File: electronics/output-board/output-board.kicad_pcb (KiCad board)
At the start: 0 parts

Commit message: Finished Schematic and Started Routing the Output Board
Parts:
- added C1: 1uF, Capacitor_SMD:C_0603_1608Metric, F.Cu at (16.4, 69.0)
- added C10: 100nF, Capacitor_SMD:C_0603_1608Metric, F.Cu at (43.5, 57.3)
- added C11: 100nF, Capacitor_SMD:C_0603_1608Metric, F.Cu at (142.2, 81.3)
- added C12: 100nF, Capacitor_SMD:C_0603_1608Metric, F.Cu at (40.4, 54.8)
- added C13: 100nF, Capacitor_SMD:C_0603_1608Metric, F.Cu at (39.5, 57.3)
- added C14: 100nF, Capacitor_SMD:C_0603_1608Metric, F.Cu at (40.4, 49.8)
- added C15: 100nF, Capacitor_SMD:C_0603_1608Metric, F.Cu at (32.0, 67.0)
- added C16: 100nF, Capacitor_SMD:C_0603_1608Metric, F.Cu at (44.4, 54.8)
- added C17: 100nF, Capacitor_SMD:C_0603_1608Metric, F.Cu at (44.4, 52.3)
- added C18: 100nF, Capacitor_SMD:C_0603_1608Metric, F.Cu at (20.4, 69.0)
- added C19: 100nF, Capacitor_SMD:C_0603_1608Metric, F.Cu at (31.5, 59.5)
- added C2: 10nF, Capacitor_SMD:C_0603_1608Metric, F.Cu at (40.4, 52.3)
- added C20: 100nF, Capacitor_SMD:C_0603_1608Metric, F.Cu at (39.5, 62.3)
- added C21: 100nF, Capacitor_SMD:C_0603_1608Metric, F.Cu at (35.5, 62.0)
- added C3: 1uF, Capacitor_SMD:C_0603_1608Metric, F.Cu at (48.4, 49.8)
- added C4: 20pF, Capacitor_SMD:C_0603_1608Metric, F.Cu at (35.5, 59.5)
- added C5: 20pF, Capacitor_SMD:C_0603_1608Metric, F.Cu at (35.1, 57.0)
- added C6: 100nF, Capacitor_SMD:C_0603_1608Metric, F.Cu at (48.4, 54.8)
- added C7: 2.2uF, Capacitor_SMD:C_0603_1608Metric, F.Cu at (39.5, 59.8)
- added C8: 2.2uF, Capacitor_SMD:C_0603_1608Metric, F.Cu at (35.5, 64.5)
- added C9: 100nF, Capacitor_SMD:C_0603_1608Metric, F.Cu at (139.2, 81.3)
- added D1: LED, LED_SMD:LED_1206_3216Metric, F.Cu at (53.8, 26.2)
- added D10: LED, LED_SMD:LED_1206_3216Metric, F.Cu at (45.9, 94.6)
- added D11: LED, LED_SMD:LED_1206_3216Metric, F.Cu at (65.2, 83.5)
- added D12: LED, LED_SMD:LED_1206_3216Metric, F.Cu at (69.4, 55.0)
- added D13: LED, LED_SMD:LED_1206_3216Metric, F.Cu at (26.7, 80.3)
- added D2: LED, LED_SMD:LED_1206_3216Metric, F.Cu at (16.8, 39.9)
- added D3: LED, LED_SMD:LED_1206_3216Metric, F.Cu at (90.2, 42.2)
- added D4: LED, LED_SMD:LED_1206_3216Metric, F.Cu at (130.0, 55.5)
- added D5: LED, LED_SMD:LED_1206_3216Metric, F.Cu at (69.4, 69.3)
- added D6: LED, LED_SMD:LED_1206_3216Metric, F.Cu at (45.9, 80.3)
- added D7: LED, LED_SMD:LED_1206_3216Metric, F.Cu at (88.6, 69.3)
- added D8: LED, LED_SMD:LED_1206_3216Metric, F.Cu at (107.9, 55.0)
- added D9: LED, LED_SMD:LED_1206_3216Metric, F.Cu at (88.6, 55.0)
- added J1: Conn_01x02_Male, Connector_Molex:Molex_SL_171971-0002_1x02_P2.54mm_Vertical, F.Cu at (49.8, 16.0)
- added J10: Conn_01x02_Male, Connector_Molex:Molex_SL_171971-0002_1x02_P2.54mm_Vertical, F.Cu at (79.8, 66.3)
- added J11: Conn_01x02_Male, Connector_Molex:Molex_SL_171971-0002_1x02_P2.54mm_Vertical, F.Cu at (99.0, 52.1)
- added J12: Conn_01x02_Male, Connector_Molex:Molex_SL_171971-0002_1x02_P2.54mm_Vertical, F.Cu at (79.8, 52.1)
- added J13: Conn_01x02_Male, Connector_Molex:Molex_SL_171971-0002_1x02_P2.54mm_Vertical, F.Cu at (37.1, 91.7)
- added J14: Arming switch, Connector_PinHeader_2.54mm:PinHeader_1x02_P2.54mm_Vertical, F.Cu at (27.1, 60.9)
- added J15: Conn_01x02_Male, Connector_Molex:Molex_SL_171971-0002_1x02_P2.54mm_Vertical, F.Cu at (56.3, 80.6)
- added J16: Conn_01x02_Male, Connector_Molex:Molex_SL_171971-0002_1x02_P2.54mm_Vertical, F.Cu at (60.5, 52.1)
- added J17: Conn_01x02_Male, Connector_Molex:Molex_SL_171971-0002_1x02_P2.54mm_Vertical, F.Cu at (17.9, 77.4)
- added J18: Conn_01x02_Male, Connector_Molex:Molex_SL_171971-0002_1x02_P2.54mm_Vertical, F.Cu at (17.4, 33.1)
- added J2: Conn_01x02_Male, Connector_Molex:Molex_SL_171971-0002_1x02_P2.54mm_Vertical, F.Cu at (81.3, 39.2)
- added J3: 12V In, Connector_PinHeader_2.54mm:PinHeader_1x02_P2.54mm_Vertical, F.Cu at (39.4, 19.3)
- added J4: Conn_01x02, Connector_PinHeader_2.54mm:PinHeader_1x02_P2.54mm_Vertical, F.Cu at (36.1, 50.8)
- added J5: SWD Header, Connector_PinHeader_2.54mm:PinHeader_1x04_P2.54mm_Vertical, F.Cu at (16.7, 50.8)
- added J6: Conn_01x02, Connector_PinHeader_2.54mm:PinHeader_1x02_P2.54mm_Vertical, F.Cu at (31.4, 50.8)
- added J7: Conn_01x02_Male, Connector_Molex:Molex_SL_171971-0002_1x02_P2.54mm_Vertical, F.Cu at (121.2, 52.6)
- added J8: Conn_01x02_Male, Connector_Molex:Molex_SL_171971-0002_1x02_P2.54mm_Vertical, F.Cu at (60.5, 66.3)
- added J9: Conn_01x02_Male, Connector_Molex:Molex_SL_171971-0002_1x02_P2.54mm_Vertical, F.Cu at (37.1, 77.4)
- added L1: 10uH, Inductor_SMD:L_0603_1608Metric, F.Cu at (31.5, 64.5)
- added MOSFET1: BSS806NEH6327XTSA1, MOSFET:BSS806NEH6327XTSA1, F.Cu at (48.8, 23.1)
- added MOSFET10: BUK9Y21-40E, MOSFET 2:BUK9Y21-40E, F.Cu at (27.7, 93.2)
- added MOSFET11: BSS806NEH6327XTSA1, MOSFET:BSS806NEH6327XTSA1, F.Cu at (65.8, 79.4)
- added MOSFET12: BSS806NEH6327XTSA1, MOSFET:BSS806NEH6327XTSA1, F.Cu at (70.0, 50.9)
- added MOSFET13: BSS806NEH6327XTSA1, MOSFET:BSS806NEH6327XTSA1, F.Cu at (27.3, 76.2)
- added MOSFET18: BSS806NEH6327XTSA1, MOSFET:BSS806NEH6327XTSA1, F.Cu at (26.9, 31.9)
- added MOSFET2: BSS806NEH6327XTSA1, MOSFET:BSS806NEH6327XTSA1, F.Cu at (90.8, 38.1)
- added MOSFET3: BSS806NEH6327XTSA1, MOSFET:BSS806NEH6327XTSA1, F.Cu at (130.6, 51.4)
- added MOSFET4: BSS806NEH6327XTSA1, MOSFET:BSS806NEH6327XTSA1, F.Cu at (70.0, 65.2)
- added MOSFET5: BSS806NEH6327XTSA1, MOSFET:BSS806NEH6327XTSA1, F.Cu at (46.5, 76.2)
- added MOSFET6: BSS806NEH6327XTSA1, MOSFET:BSS806NEH6327XTSA1, F.Cu at (89.2, 65.2)
- added MOSFET7: BSS806NEH6327XTSA1, MOSFET:BSS806NEH6327XTSA1, F.Cu at (108.5, 50.9)
- added MOSFET8: BSS806NEH6327XTSA1, MOSFET:BSS806NEH6327XTSA1, F.Cu at (89.2, 50.9)
- added MOSFET9: BSS806NEH6327XTSA1, MOSFET:BSS806NEH6327XTSA1, F.Cu at (46.5, 90.5)
- added R1: 0k, Resistor_SMD:R_0603_1608Metric, F.Cu at (48.4, 52.3)
- added R10: 500, Resistor_SMD:R_0603_1608Metric, F.Cu at (82.4, 58.4)
- added R11: 500, Resistor_SMD:R_0603_1608Metric, F.Cu at (39.7, 98.0)
- added R12: 1K, Resistor_SMD:R_0603_1608Metric, F.Cu at (31.1, 57.0)
- added R13: 100K, Resistor_SMD:R_0603_1608Metric, F.Cu at (32.0, 69.5)
- added R14: 1K, Resistor_SMD:R_0603_1608Metric, F.Cu at (74.1, 78.3)
- added R15: 1K, Resistor_SMD:R_0603_1608Metric, F.Cu at (48.8, 27.2)
- added R16: 1K, Resistor_SMD:R_0603_1608Metric, F.Cu at (95.1, 36.9)
- added R17: 1K, Resistor_SMD:R_0603_1608Metric, F.Cu at (134.9, 50.3)
- added R18: 1K, Resistor_SMD:R_0603_1608Metric, F.Cu at (59.1, 72.7)
- added R19: 1K, Resistor_SMD:R_0603_1608Metric, F.Cu at (35.7, 83.8)
- added R2: 500, Resistor_SMD:R_0603_1608Metric, F.Cu at (54.4, 22.4)
- added R20: 500, Resistor_SMD:R_0603_1608Metric, F.Cu at (25.4, 35.6)
- added R21: 1K, Resistor_SMD:R_0603_1608Metric, F.Cu at (78.3, 72.7)
- added R22: 1K, Resistor_SMD:R_0603_1608Metric, F.Cu at (97.6, 58.4)
- added R23: 1K, Resistor_SMD:R_0603_1608Metric, F.Cu at (78.3, 58.4)
- added R24: 1K, Resistor_SMD:R_0603_1608Metric, F.Cu at (35.7, 98.0)
- added R25: 1K, Resistor_SMD:R_0603_1608Metric, F.Cu at (54.9, 86.9)
- added R26: 500, Resistor_SMD:R_0603_1608Metric, F.Cu at (58.9, 86.9)
- added R27: 1K, Resistor_SMD:R_0603_1608Metric, F.Cu at (59.1, 58.4)
- added R28: 500, Resistor_SMD:R_0603_1608Metric, F.Cu at (63.1, 58.4)
- added R29: 1K, Resistor_SMD:R_0603_1608Metric, F.Cu at (16.4, 83.8)
- added R3: 10k, Resistor_SMD:R_0603_1608Metric, F.Cu at (31.5, 62.0)
- added R30: 500, Resistor_SMD:R_0603_1608Metric, F.Cu at (20.4, 83.8)
- added R4: 500, Resistor_SMD:R_0603_1608Metric, F.Cu at (89.3, 45.1)
- added R5: 500, Resistor_SMD:R_0603_1608Metric, F.Cu at (129.1, 58.4)
- added R6: 500, Resistor_SMD:R_0603_1608Metric, F.Cu at (63.1, 72.7)
- added R7: 500, Resistor_SMD:R_0603_1608Metric, F.Cu at (39.7, 83.8)
- added R8: 500, Resistor_SMD:R_0603_1608Metric, F.Cu at (82.4, 72.7)
- added R9: 500, Resistor_SMD:R_0603_1608Metric, F.Cu at (101.6, 58.4)
- added SW1: SW_Push_Dual, RESET BUTTON:Button CS1102, F.Cu at (19.6, 64.3)
- added U1: MAX33012EASA+, MAX33012EASA+:MAX33012EASA+, F.Cu at (56.4, 42.4)
- added U2: LD3985M33R_SOT23, Package_TO_SOT_SMD:SOT-23-5, F.Cu at (27.4, 68.0)
- added U3: STM32F446ZEHx, Package_BGA:UFBGA-144_7x7mm_Layout12x12_P0.5mm, F.Cu at (142.2, 88.9)
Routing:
- net Net-(D1-Pad1): track 0.00 -> 14.7 mm
- net +12V: track 0.00 -> 9.62 mm
- net Net-(D1-Pad2): track 0.00 -> 3.84 mm
- net Net-(MOSFET1-Pad1): track 0.00 -> 2.78 mm
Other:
- copper layers 0 -> 2

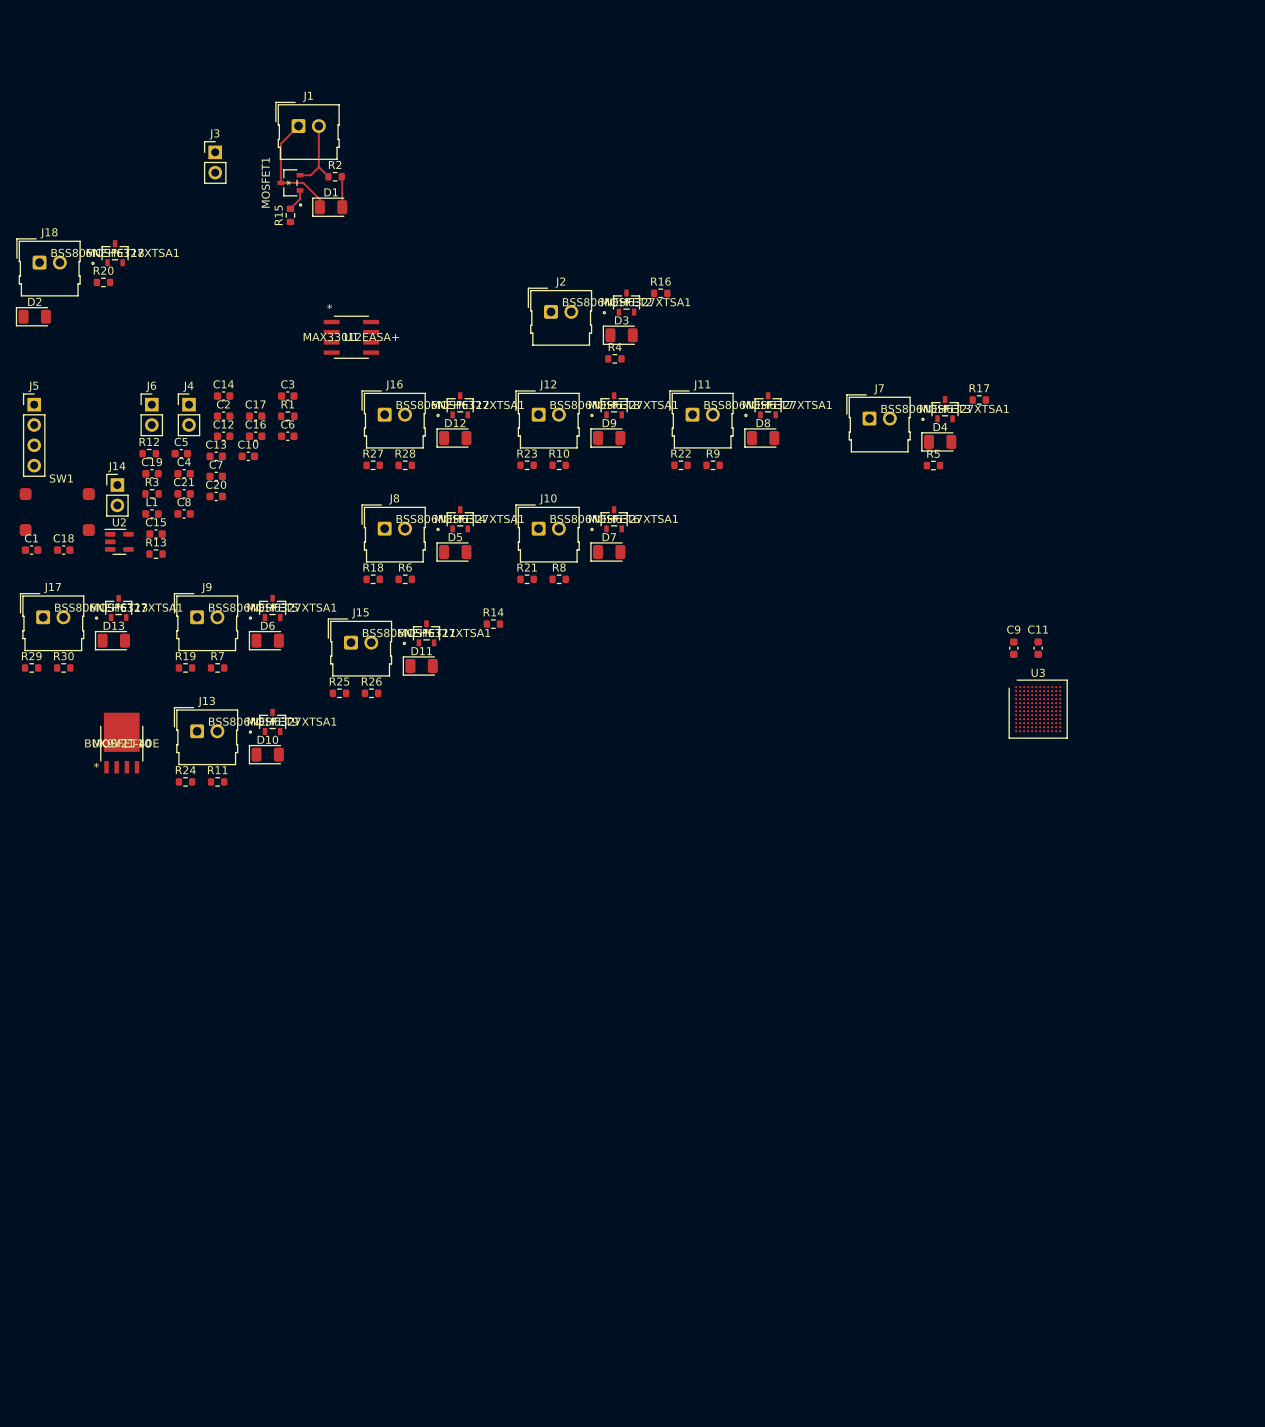
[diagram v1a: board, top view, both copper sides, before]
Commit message: Output Board is basically done!
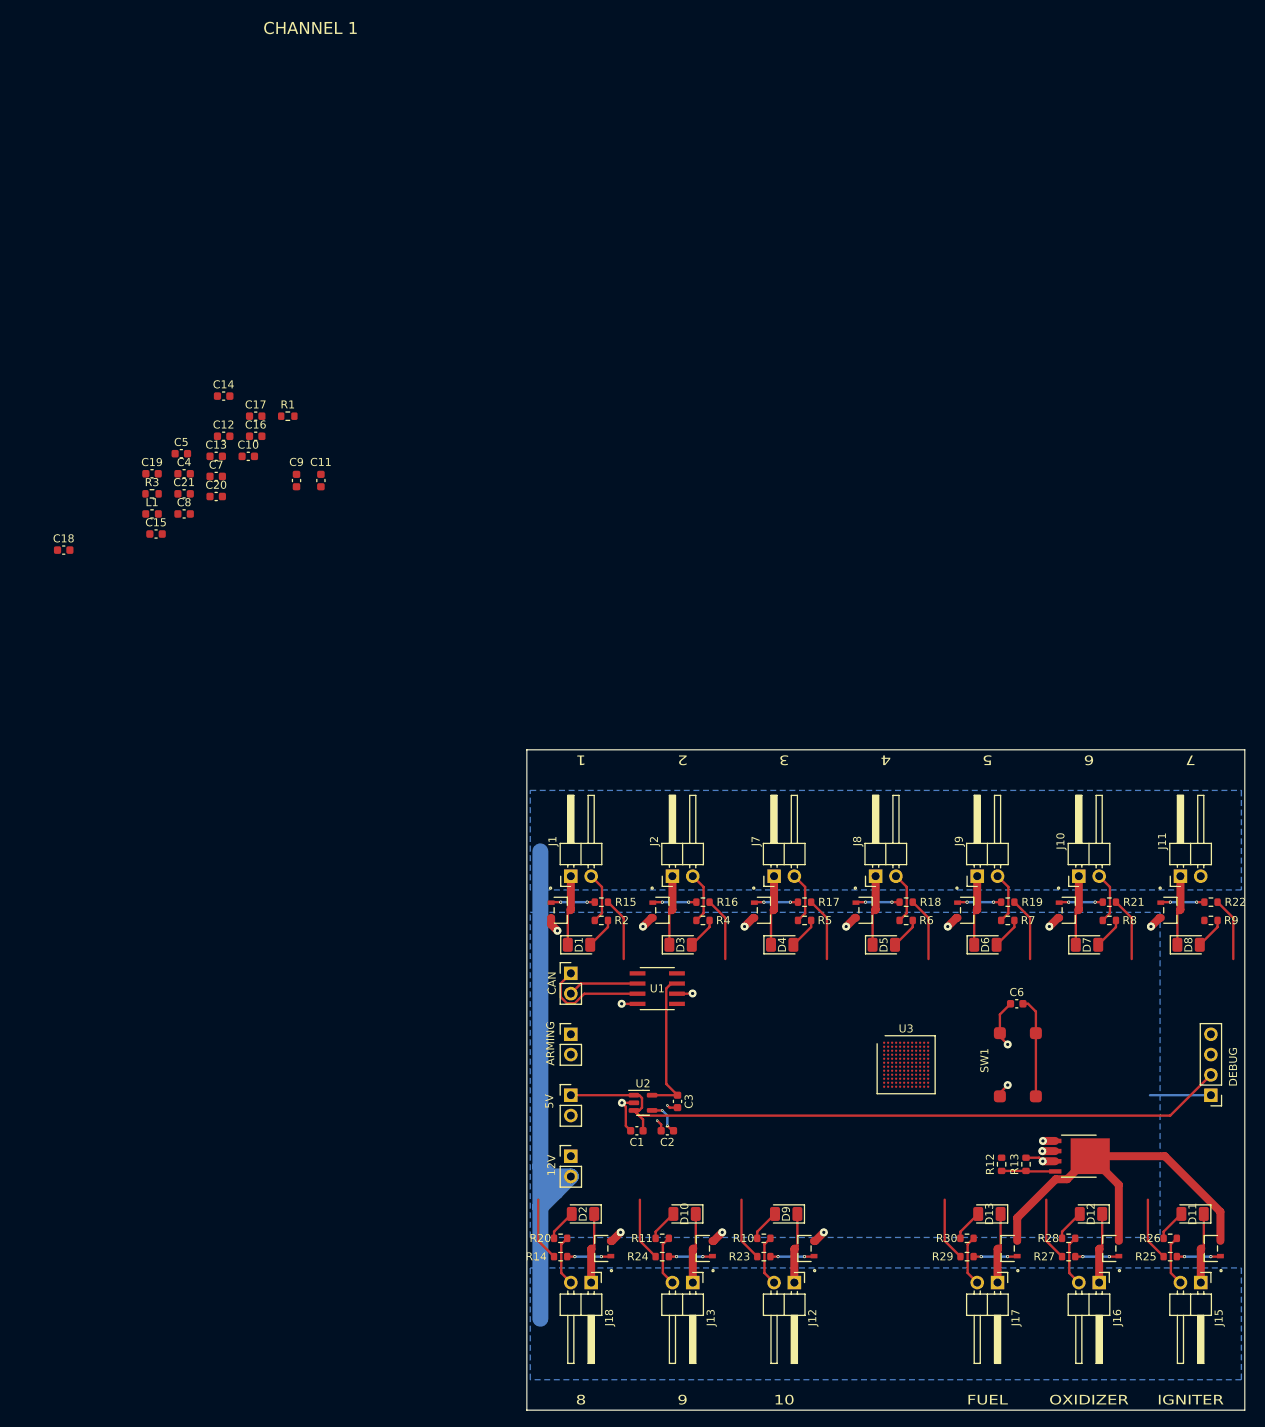
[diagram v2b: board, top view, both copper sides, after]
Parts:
- J1, J10, J11, J12, J13, J15, J16, J17, J18, J2, J7, J8, J9: footprint Connector_Molex:Molex_SL_171971-0002_1x02_P2.54mm_Vertical -> Connector_PinHeader_2.54mm:PinHeader_1x02_P2.54mm_Horizontal
- J14: value Arming switch -> ARMING
- J3: value 12V In -> 12V
- J4: value Conn_01x02 -> 5V
- J5: value SWD Header -> DEBUG
- J6: value Conn_01x02 -> CAN
- moved J5 170.5 mm to (163.8, 137.2), turned to 180 degrees
- moved J17 145.4 mm to (137.2, 160.6), turned to -90 degrees
- moved J18 144.9 mm to (86.4, 160.6), turned to -90 degrees
- moved J16 140.5 mm to (149.9, 160.6), turned to -90 degrees
- moved R12 138.7 mm to (137.7, 145.8), turned to 90 degrees
- moved SW1 138.5 mm to (139.7, 133.3), turned to 90 degrees
- moved MOSFET18 138.5 mm to (87.6, 156.3), turned to 90 degrees
- moved R29 138.2 mm to (133.3, 157.3)
- moved MOSFET13 137.0 mm to (138.4, 156.3), turned to 90 degrees
- moved R30 133.5 mm to (133.3, 155.0), turned to 180 degrees
- moved J3 133.1 mm to (83.8, 144.8)
- moved MOSFET12 133.0 mm to (151.1, 156.3), turned to 90 degrees
- moved J15 133.0 mm to (162.6, 160.6), turned to -90 degrees
- moved R13 132.8 mm to (140.7, 145.8), turned to 90 degrees
- moved R20 132.5 mm to (82.5, 155.0), turned to 180 degrees
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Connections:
- MOSFET1 pad 2: +12V -> GND
- MOSFET18 pad 2: +12V -> GND
- MOSFET2 pad 2: +12V -> GND
- MOSFET3 pad 2: +12V -> GND
- MOSFET4 pad 2: +12V -> GND
- MOSFET5 pad 2: +12V -> GND
- MOSFET6 pad 2: +12V -> GND
- MOSFET7 pad 2: +12V -> GND
- MOSFET8 pad 2: +12V -> GND
- MOSFET9 pad 2: +12V -> GND
- R13 pad 1: Net-(J14-Pad1) -> Net-(MOSFET10-Pad4)
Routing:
- net +12V: track 9.62 -> 147.1 mm
- net +5V: track 0.00 -> 88.9 mm
- net GND: track 0.00 -> 51.7 mm, vias 0 -> 20
- net /Ignition MOSFET/GROUND: track 0.00 -> 50.1 mm
- net +3V3: track 0.00 -> 18.7 mm
- net Net-(J6-Pad1): track 0.00 -> 13.9 mm
- net Net-(C6-Pad2): track 0.00 -> 12.6 mm
- net Net-(J6-Pad2): track 0.00 -> 8.86 mm
- net Net-(D2-Pad1): track 0.00 -> 8.74 mm
- net Net-(D8-Pad1): track 0.00 -> 8.74 mm
- net Net-(D12-Pad1): track 0.00 -> 8.74 mm
- net Net-(D9-Pad1): track 0.00 -> 8.74 mm
- net Net-(D13-Pad1): track 0.00 -> 8.74 mm
- net Net-(D11-Pad1): track 0.00 -> 8.74 mm
- net Net-(D10-Pad1): track 0.00 -> 8.74 mm
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- added copper zone on B.Cu, net +12V
- added copper zone on B.Cu, net GND
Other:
- board outline added: 89.7 x 82.5 mm
- board text added: "1"
- board text added: "10"
- board text added: "2"
- board text added: "3"
- board text added: "4"
- board text added: "5"
- board text added: "6"
- board text added: "7"
- board text added: "8"
- board text added: "9"
- board text added: "CHANNEL 1"
- board text added: "FUEL"
- board text added: "IGNITER"
- board text added: "OXIDIZER"

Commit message: Put in connectors and finalized layout of everything except MCU.
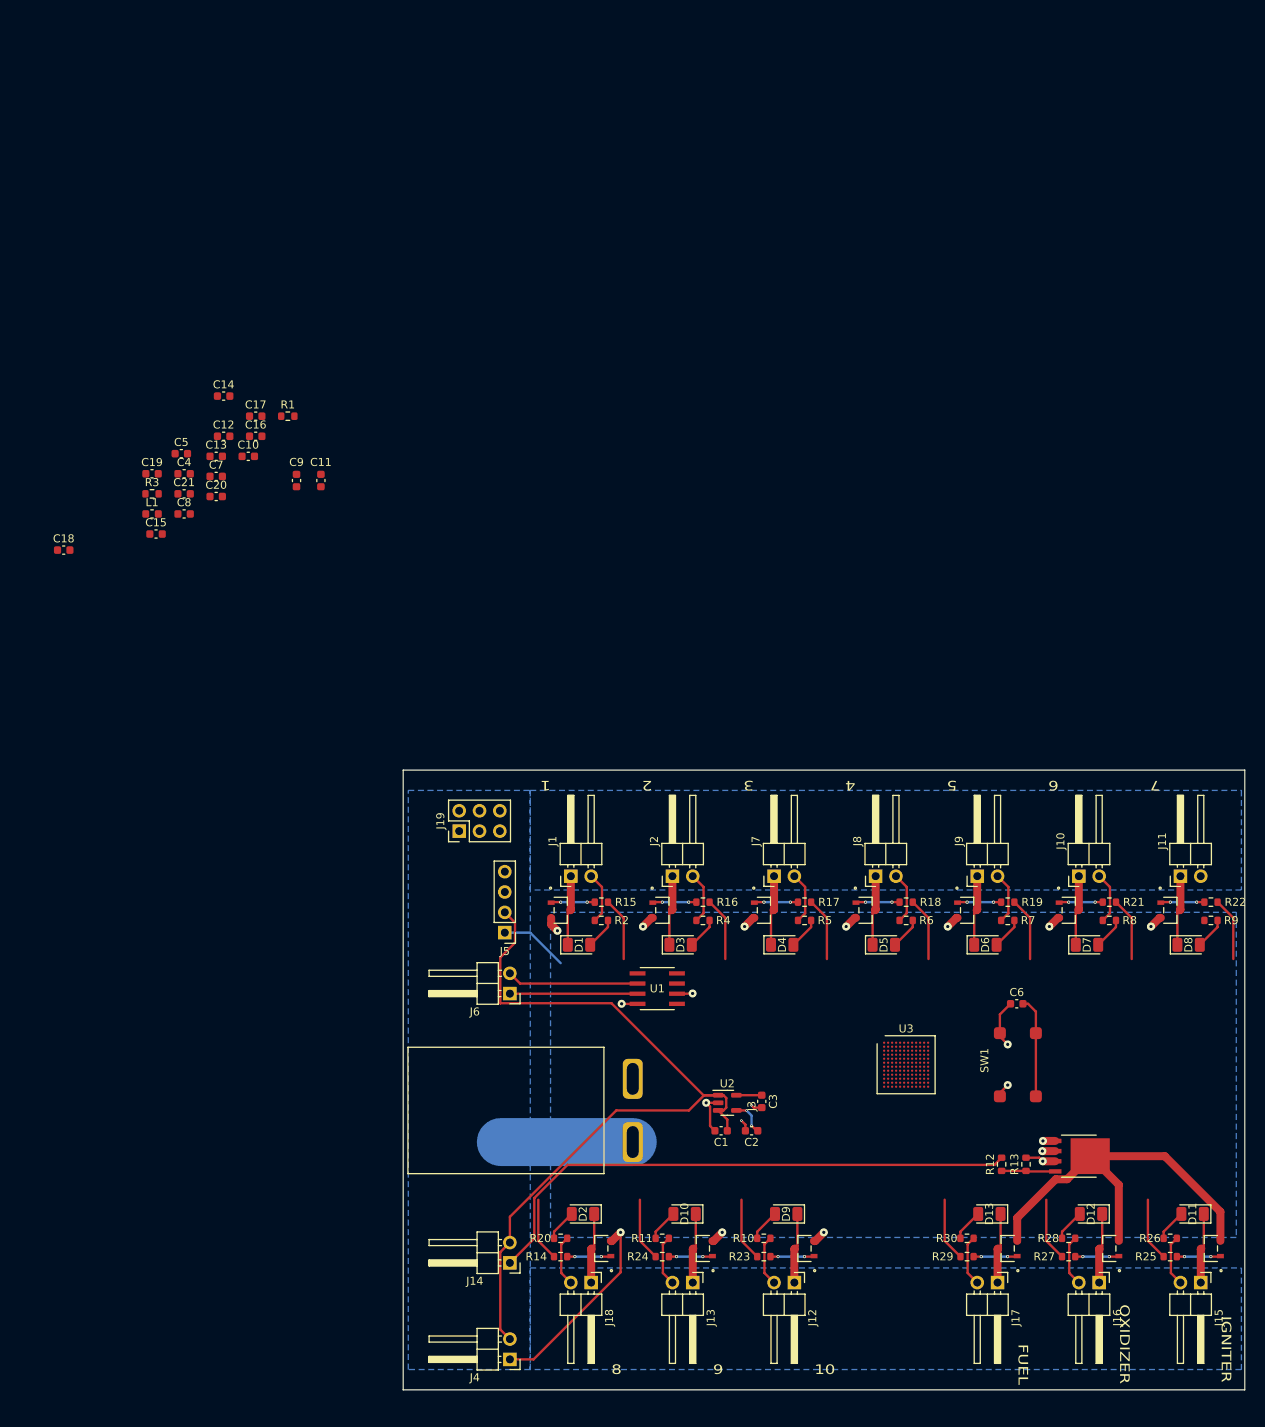
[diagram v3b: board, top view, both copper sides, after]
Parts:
- added J19: Extra IO, Connector_PinHeader_2.54mm:PinHeader_2x03_P2.54mm_Vertical, F.Cu at (69.9, 104.1)
- J1, J10, J11, J12, J13, J15, J16, J17, J18, J2, J7, J8, J9: footprint Connector_PinHeader_2.54mm:PinHeader_1x02_P2.54mm_Horizontal -> CustomFootprints:LatchingConnector2POS
- J14: value ARMING -> Arming switch; footprint Connector_PinHeader_2.54mm:PinHeader_1x02_P2.54mm_Vertical -> CustomFootprints:LatchingConnector2POS
- J3: value 12V -> 12V In; footprint Connector_PinHeader_2.54mm:PinHeader_1x02_P2.54mm_Vertical -> CustomFootprints:PowerPoleThroughHole
- J4: value 5V -> Conn_01x02; footprint Connector_PinHeader_2.54mm:PinHeader_1x02_P2.54mm_Vertical -> CustomFootprints:LatchingConnector2POS
- J5: value DEBUG -> SWD Header
- J6: value CAN -> Conn_01x02; footprint Connector_PinHeader_2.54mm:PinHeader_1x02_P2.54mm_Vertical -> CustomFootprints:LatchingConnector2POS
- moved J5 90.6 mm to (75.6, 116.8)
- moved J4 33.9 mm to (76.2, 170.2), turned to 180 degrees
- moved J14 29.6 mm to (76.2, 158.1), turned to 180 degrees
- moved C1 10.5 mm to (102.6, 141.6)
- moved C2 10.5 mm to (106.4, 141.6)
- moved C3 10.5 mm to (107.7, 137.9)
- moved U2 10.5 mm to (103.4, 138.1)
- moved J3 9.62 mm to (91.6, 139.1), turned to 90 degrees
- moved J6 8.03 mm to (76.2, 124.5), turned to 180 degrees
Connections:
- J4 pad 1: +5V -> GND
- J4 pad 2: GND -> +5V
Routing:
- net Net-(J14-Pad1): track 0.00 -> 69.9 mm
- net +12V: track 147.1 -> 93.3 mm
- net GND: track 51.7 -> 76.0 mm
- net +3V3: track 18.7 -> 3.17 mm
- net +5V: track 88.9 -> 99.8 mm
- net Net-(J6-Pad2): track 8.86 -> 16.5 mm
- net Net-(J6-Pad1): track 13.9 -> 16.0 mm
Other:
- board size 89.7 x 82.5 mm -> 105.2 x 77.5 mm
- board text removed: "CHANNEL 1"
